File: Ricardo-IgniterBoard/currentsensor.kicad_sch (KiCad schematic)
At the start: 1 part, among them U2 INA219AxDCN

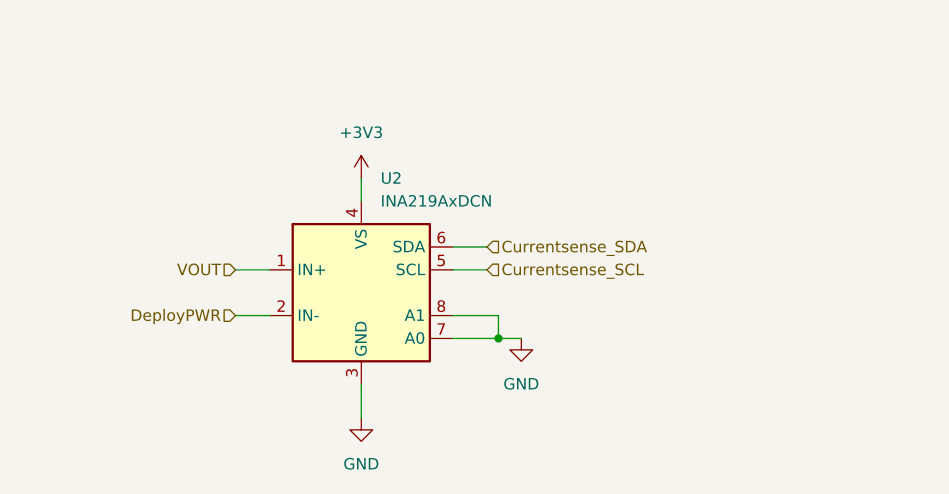
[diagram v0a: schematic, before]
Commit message: input filter
added to current sensor
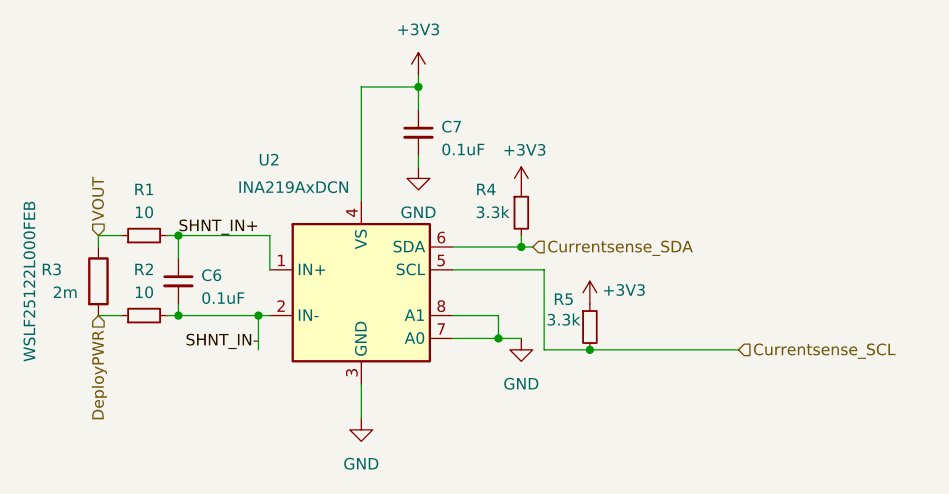
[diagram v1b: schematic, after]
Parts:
- added C6, C7: 0.1uF, Capacitor_SMD:C_0402_1005Metric, symbol Device:C_Small
- added R1, R2: 10, Resistor_SMD:R_0402_1005Metric, symbol Device:R_Small
- added R3: 2m, Resistor_SMD:R_2512_6332Metric_Pad1.40x3.35mm_HandSolder, symbol Device:R
- added R4, R5: 3.3k, Resistor_SMD:R_0402_1005Metric, symbol Device:R_Small
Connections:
- net +3V3: now also C7.1, R4.1, R5.1
- net Currentsense_SCL: now also R5.2
- net Currentsense_SDA: now also R4.2
- net DeployPWR: now also R2.1, R3.2; no longer U2.2 (IN-)
- net GND: now also C7.2
- net VOUT: now also R1.1, R3.1; no longer U2.1 (IN+)
- new net SHNT_IN+: C6.1, R1.2, U2.1 (IN+)
- new net SHNT_IN-: C6.2, R2.2, U2.2 (IN-)

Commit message: added test points on input filter
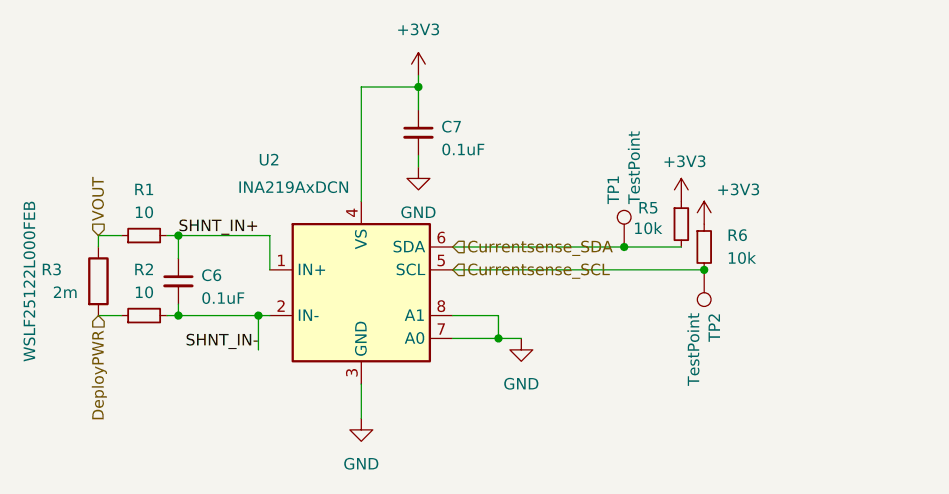
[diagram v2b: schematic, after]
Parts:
- removed R4: 3.3k, Resistor_SMD:R_0402_1005Metric, symbol Device:R_Small
- added R6: 10k, Resistor_SMD:R_0402_1005Metric, symbol Device:R_Small
- added TP1, TP2: TestPoint, TestPoint:TestPoint_Pad_D1.0mm, symbol Connector:TestPoint
- R5: value 3.3k -> 10k
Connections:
- net +3V3: now also R6.1
- net Currentsense_SCL: now also R6.2, TP2.1; no longer R5.2
- net Currentsense_SDA: now also R5.2, TP1.1
